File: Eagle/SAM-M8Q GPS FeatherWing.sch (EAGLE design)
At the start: 24 parts, among them Q1 DMG3415U-7, Q2 2N2222, SW1 KMR2, U1 SAM-M8Q

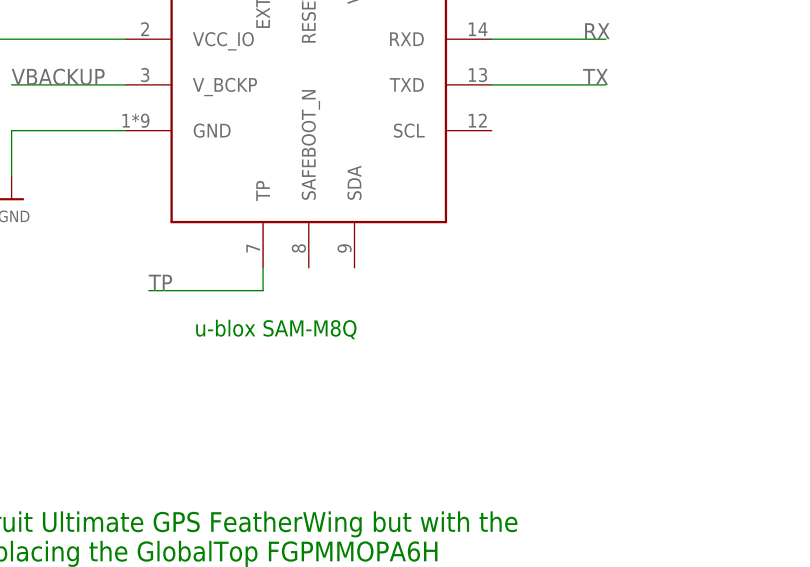
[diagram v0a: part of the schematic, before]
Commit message: Reduced vias. Added pad for SAFEBOOT.
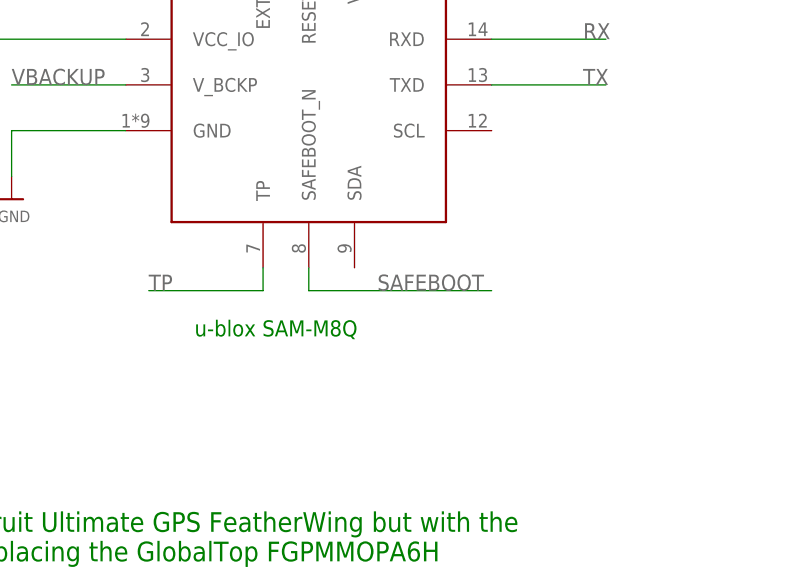
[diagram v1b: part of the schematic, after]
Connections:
- new net SAFEBOOT: U1.SAFEBOOT_N
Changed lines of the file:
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@@
+</segment>
+</net>
+<net name="SAFEBOOT" class="0">
+<segment>
+<pinref part="U1" gate="G$1" pin="SAFEBOOT_N"/>
+<wire x1="193.04" y1="93.98" x2="193.04" y2="91.44" width="0.1524" layer="91"/>
+<label x="200.66" y="91.44" size="1.778" layer="95"/>
+<wire x1="193.04" y1="91.44" x2="213.36" y2="91.44" width="0.1524" layer="91"/>
 </segment>
 </net>

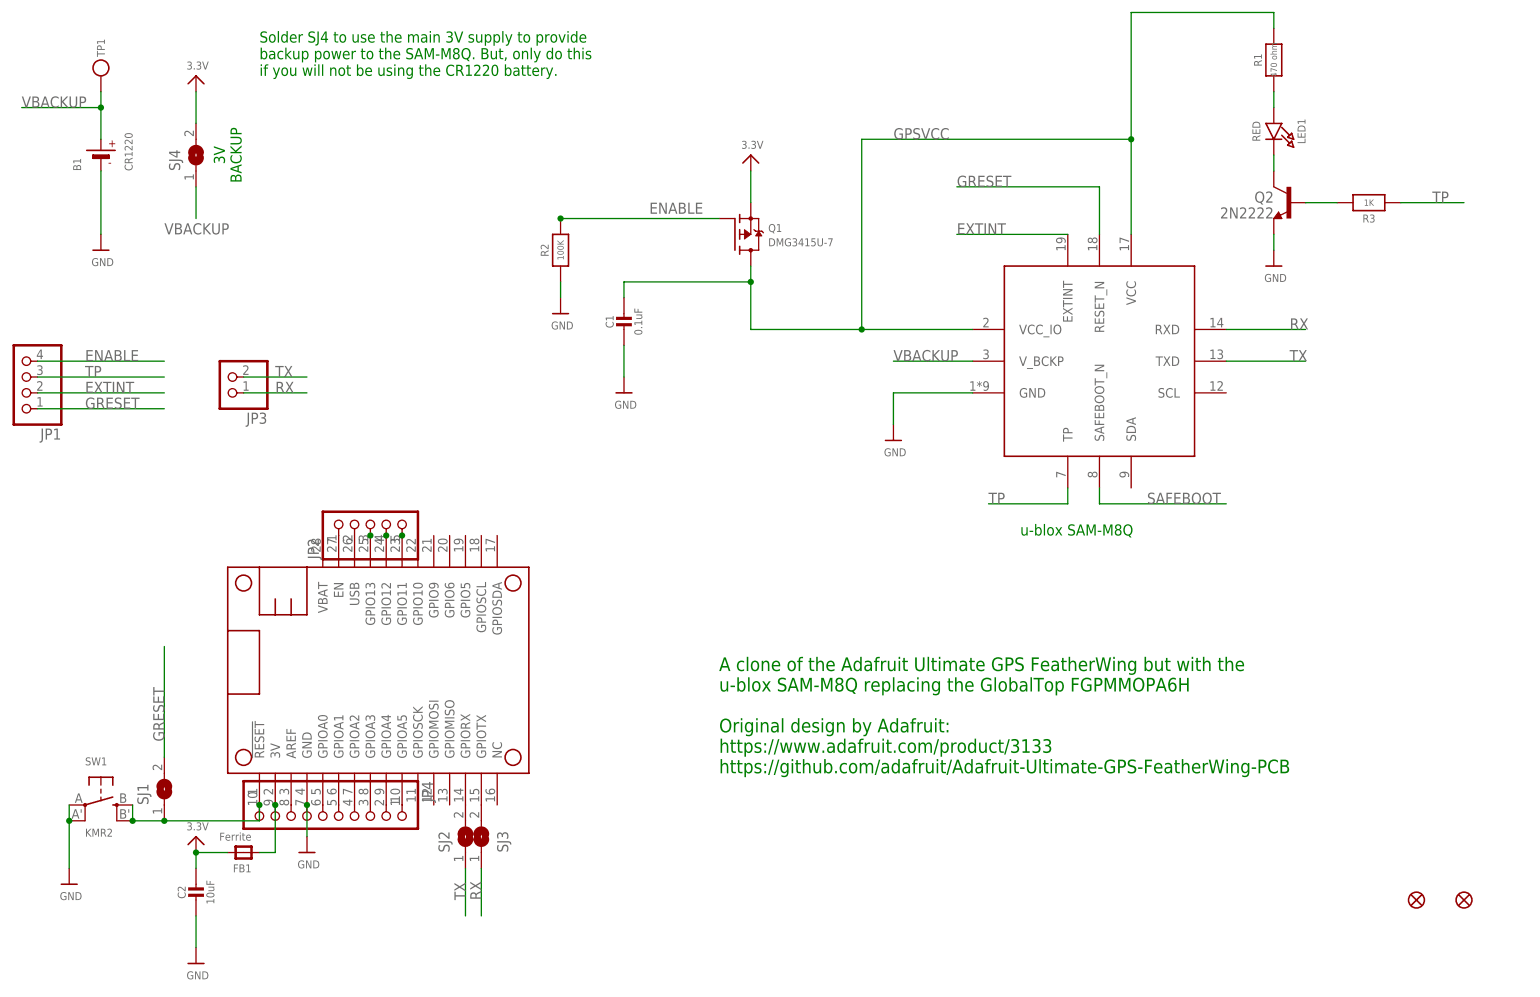
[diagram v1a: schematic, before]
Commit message: Added a test pad for safeboot
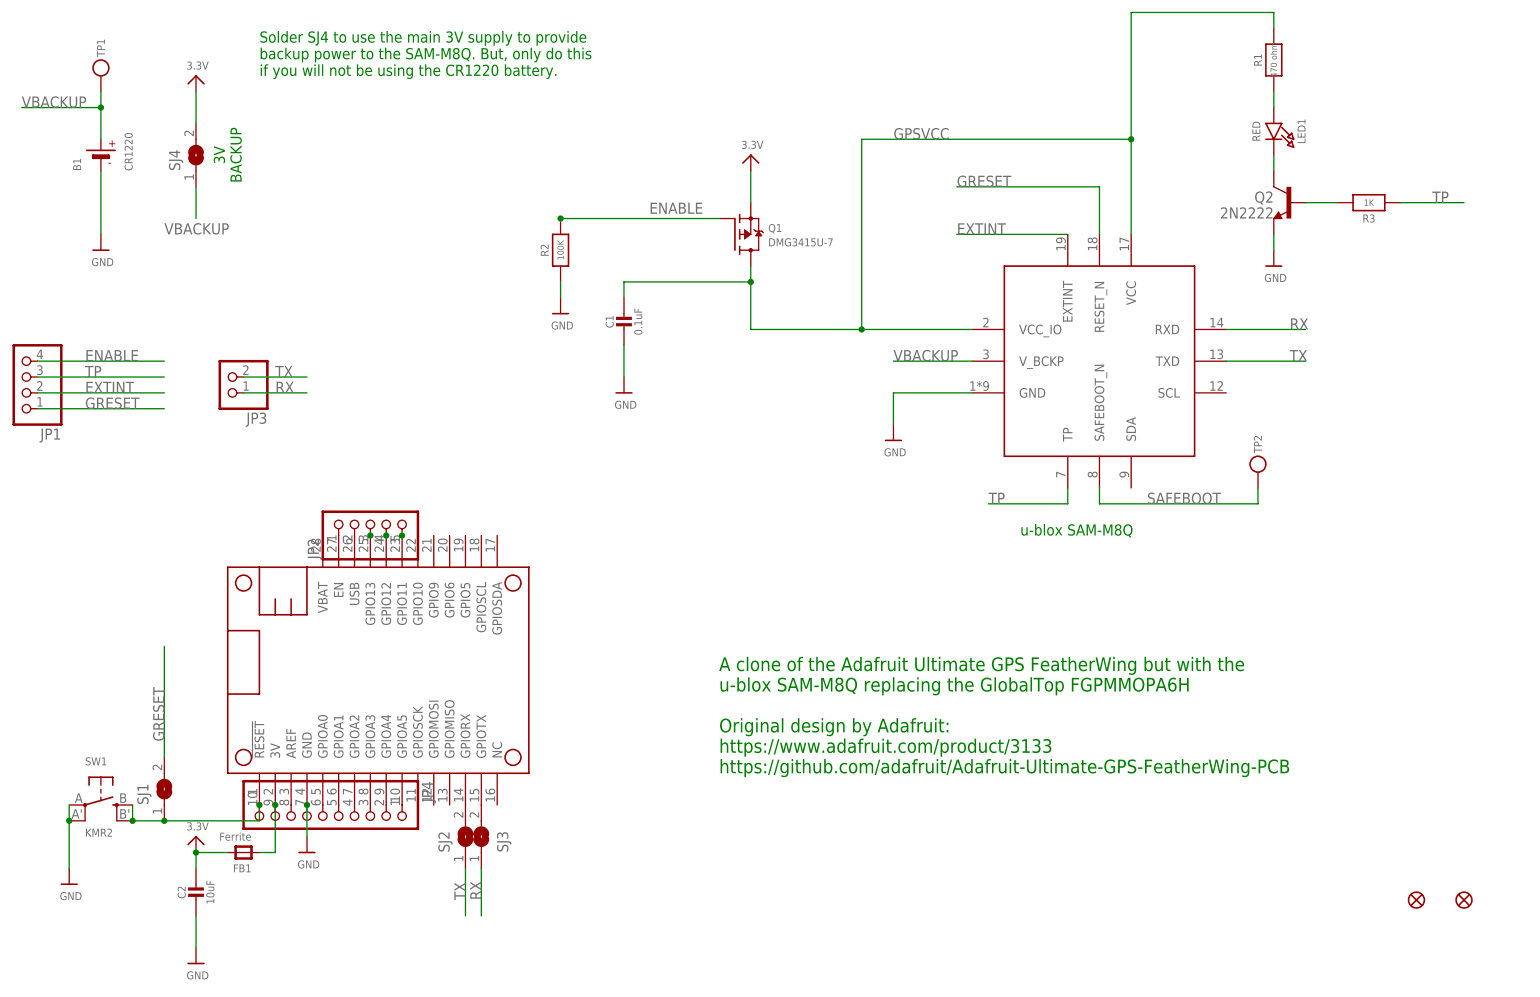
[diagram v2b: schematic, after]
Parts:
- added TP2: (no value), microbuilder:TESTPOINTROUND1.5MM
- SJ4: device jumper:SJ -> microbuilder:SOLDERJUMPER
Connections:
- net SAFEBOOT: now also TP2.P$1
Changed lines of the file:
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@@
 <?xml version="1.0" encoding="utf-8"?>
 <!DOCTYPE eagle SYSTEM "eagle.dtd">
-<eagle version="8.2.2">
+<eagle version="8.3.2">
 <drawing>
 <settings>
 <setting alwaysvectorfont="yes"/>
+<setting keepoldvectorfont="yes"/>
 <setting verticaltext="up"/>
 </settings>
@@
 <part name="U$12" library="microbuilder" deviceset="GND" device=""/>
 <part name="R3" library="microbuilder" deviceset="RESISTOR" device="0805_NOOUTLINE" value="1K"/>
-<part name="SJ4" library="jumper" deviceset="SJ" device=""/>
 <part name="U$9" library="microbuilder" deviceset="3.3V" device=""/>
+<part name="TP2" library="microbuilder" deviceset="TESTPOINT" device="ROUND1.5MM"/>
+<part name="SJ4" library="microbuilder" deviceset="SOLDERJUMPER" device=""/>
 </parts>
 <sheets>
@@
 <instance part="U$12" gate="G$1" x="220.98" y="129.54"/>
 <instance part="R3" gate="G$1" x="236.22" y="139.7" rot="R180"/>
+<instance part="U$9" gate="G$1" x="48.26" y="160.02"/>
+<instance part="TP2" gate="G$1" x="218.44" y="93.98"/>
 <instance part="SJ4" gate="1" x="48.26" y="147.32" rot="R90"/>
-<instance part="U$9" gate="G$1" x="48.26" y="160.02"/>
 </instances>
 <busses>
@@
 <pinref part="U$9" gate="G$1" pin="3.3V"/>
 <pinref part="SJ4" gate="1" pin="2"/>
-<wire x1="48.26" y1="157.48" x2="48.26" y2="152.4" width="0.1524" layer="91"/>
+<wire x1="48.26" y1="152.4" x2="48.26" y2="157.48" width="0.1524" layer="91"/>
 </segment>
 </net>
@@
 </segment>
 <segment>
+<label x="43.18" y="134.62" size="1.778" layer="95"/>
 <pinref part="SJ4" gate="1" pin="1"/>
 <wire x1="48.26" y1="142.24" x2="48.26" y2="137.16" width="0.1524" layer="91"/>
-<label x="43.18" y="134.62" size="1.778" layer="95"/>
 </segment>
 </net>
@@
 <wire x1="193.04" y1="93.98" x2="193.04" y2="91.44" width="0.1524" layer="91"/>
 <label x="200.66" y="91.44" size="1.778" layer="95"/>
-<wire x1="193.04" y1="91.44" x2="213.36" y2="91.44" width="0.1524" layer="91"/>
-</segment>
-</net>
+<wire x1="193.04" y1="91.44" x2="218.44" y2="91.44" width="0.1524" layer="91"/>
+<pinref part="TP2" gate="G$1" pin="P$1"/>
+<wire x1="218.44" y1="91.44" x2="218.44" y2="93.98" width="0.1524" layer="91"/>
+</segment>
+</net>
